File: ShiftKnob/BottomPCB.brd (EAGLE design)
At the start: 38.1 x 38 mm, 38 parts, among them IC2 UA78M05DCY, J1 AVR_SPI_PRG_6PTH, Q1 16MHz, Q2 MOSFET-NCHANNELSMD, Q3 MOSFET-PCHANNELSMD, Q4 MOSFET-NCHANNELSMD, Q5 MOSFET-NCHANNELSMD, Q6 MOSFET-NCHANNELSMD, U1 ATMEGA328, U3 FT232RL-BASICSSOP

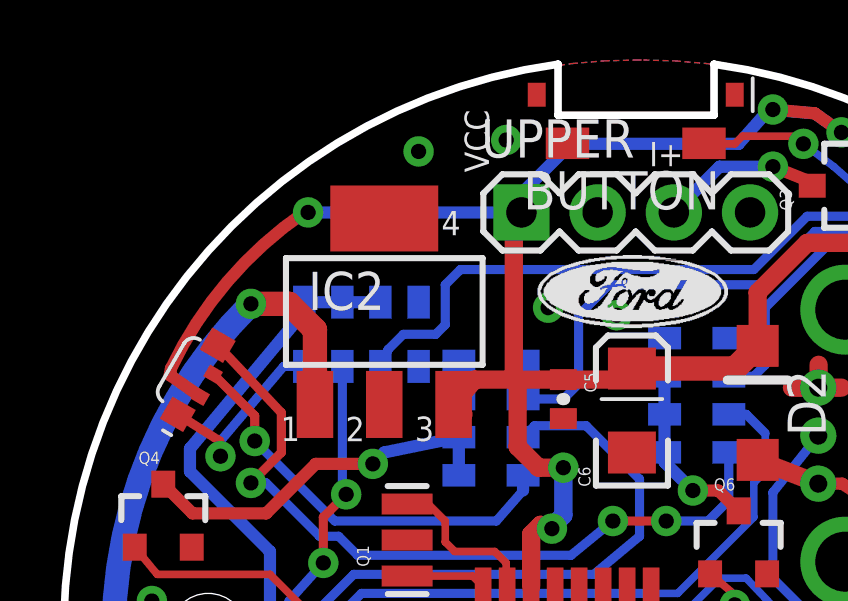
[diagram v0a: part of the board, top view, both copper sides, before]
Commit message: move silk screens for better visibility.
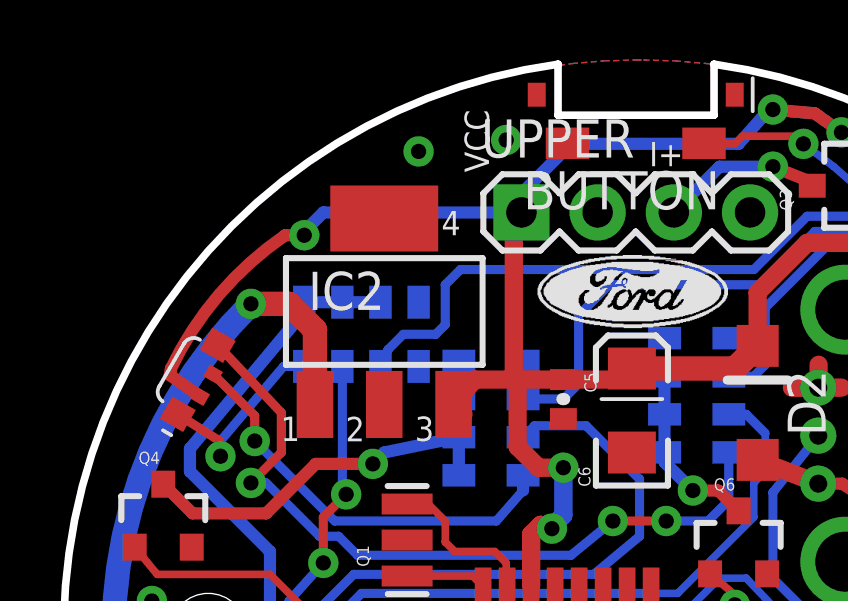
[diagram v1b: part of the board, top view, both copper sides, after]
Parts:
- moved U$3 4.27 mm to (17.7, 19.0)
- renumbered U$6 to U6
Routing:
- net GND: vias 21 -> 19
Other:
- board text added: "v02"
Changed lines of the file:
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@@
 <text x="21.778" y="6.162" size="0.8128" layer="21" rot="R180" align="bottom-right">SER</text>
 <text x="24.1402" y="22.8498" size="1.778" layer="22" rot="MR0">ZNELSON1</text>
-<text x="26.7056" y="13.3248" size="1.778" layer="22" rot="MR0">4.05.13</text>
+<text x="26.3246" y="32.5018" size="1.778" layer="22" rot="MR0">4.05.13</text>
 <rectangle x1="21.0033" y1="19.8907" x2="21.6129" y2="19.9161" layer="22" rot="R180"/>
 <rectangle x1="20.6223" y1="19.9161" x2="22.0193" y2="19.9415" layer="22" rot="R180"/>
@@
 <rectangle x1="20.5969" y1="22.2783" x2="22.0447" y2="22.3037" layer="22" rot="R180"/>
 <rectangle x1="21.0033" y1="22.3037" x2="21.6383" y2="22.3291" layer="22" rot="R180"/>
-<text x="14.671" y="33.594" size="0.8128" layer="22" rot="MR0">100Ω</text>
-<text x="15.174" y="32.319" size="0.8128" layer="22" rot="MR180">100Ω</text>
-<text x="25.085" y="32.324" size="0.8128" layer="22" rot="MR0">150Ω</text>
+<text x="14.798" y="33.467" size="0.8128" layer="22" rot="MR0">100Ω</text>
+<text x="14.92" y="29.276" size="0.8128" layer="22" rot="SMR270">100Ω</text>
+<text x="21.778" y="31.816" size="0.8128" layer="22" rot="SMR270">150Ω</text>
 <rectangle x1="57.3888" y1="23.5102" x2="57.9984" y2="23.5356" layer="49" rot="R90"/>
 <rectangle x1="56.9697" y1="23.4975" x2="58.3667" y2="23.5229" layer="49" rot="R90"/>
@@
 <text x="34.351" y="21.275" size="0.8128" layer="21" rot="R90">TX</text>
 <text x="30.795" y="21.275" size="0.8128" layer="21" rot="R90">RX</text>
+<text x="27.3406" y="17.8968" size="1.778" layer="22" rot="MR0">v02</text>
 </plain>
 <attributes>
@@
 <element name="U1" library="SparkFun" package="TQFP32-08" value="ATMEGA328" x="19.304" y="18.796" rot="R270"/>
 <element name="C2" library="SparkFun" package="0402-CAP" value="0.1uF" x="23.495" y="12.7"/>
-<element name="U$3" library="SparkFun" package="OSHW-LOGO-S" value="OSHW-LOGOS" x="21.3716" y="16.8046" rot="MR0"/>
+<element name="U$3" library="SparkFun" package="OSHW-LOGO-S" value="OSHW-LOGOS" x="17.6886" y="18.9636" rot="MR0"/>
 <element name="JP3" library="SparkFun-Connectors" package="1X02" value="12V Vehicle Connection" x="5.842" y="17.526" rot="MR270"/>
 <element name="LED2" library="FORD_frames" package="LED-RGB_SMD-RIGHTANGLE" value="LED-RGB" x="21.59" y="4.572" rot="R180"/>
@@
 <element name="J1" library="SparkFun-Connectors" package="2X3" value="AVR_SPI_PRG_6PTH" x="9.398" y="12.319" rot="R315"/>
 <element name="U3" library="SparkFun-DigitalIC" package="SSOP28DB" value="FT232RL-BASICSSOP" x="30.226" y="15.113" rot="R270"/>
-<element name="U$6" library="FORD_frames" package="USB-MINI-B_VERTICAL" value="USB-MINI-B_VERTICAL" x="28.575" y="28.1178" rot="MR0"/>
+<element name="U6" library="FORD_frames" package="USB-MINI-B_VERTICAL" value="USB-MINI-B_VERTICAL" x="28.575" y="28.1178" rot="MR0"/>
 <element name="R13" library="SparkFun" package="0402-RES" value="10K" x="32.893" y="24.638" rot="R90"/>
 <element name="R14" library="SparkFun" package="0402-RES" value="10K" x="31.496" y="24.638" rot="R90"/>
@@
 <contactref element="U3" pad="18"/>
 <contactref element="U3" pad="21"/>
-<contactref element="U$6" pad="GND"/>
+<contactref element="U6" pad="GND"/>
 <contactref element="C10" pad="C"/>
 <contactref element="IC2" pad="4"/>
@@
 <via x="14.351" y="37.592" extent="1-16" drill="0.508"/>
 <via x="17.272" y="37.973" extent="1-16" drill="0.508"/>
-<via x="20.955" y="32.131" extent="1-16" drill="0.508"/>
-<via x="18.669" y="32.385" extent="1-16" drill="0.508"/>
 <via x="31.496" y="30.861" extent="1-16" drill="0.508"/>
 <wire x1="27.686" y1="29.718" x2="26.797" y2="29.718" width="0.6096" layer="1"/>
@@
 <wire x1="19.431" y1="37.846" x2="17.78" y2="36.195" width="0.4064" layer="16"/>
 <wire x1="17.78" y1="36.195" x2="17.78" y2="35.56" width="0.4064" layer="16"/>
-<wire x1="10.668" y1="35.56" x2="17.78" y2="35.56" width="0.4064" layer="16"/>
+<wire x1="10.541" y1="34.798" x2="10.541" y2="34.925" width="0.4064" layer="16"/>
+<wire x1="10.541" y1="34.925" x2="11.176" y2="35.56" width="0.4064" layer="16"/>
+<wire x1="11.176" y1="35.56" x2="17.78" y2="35.56" width="0.4064" layer="16"/>
 <wire x1="25.654" y1="31.11" x2="24.9" y2="30.356" width="0.8128" layer="1"/>
 <wire x1="24.9" y1="30.356" x2="21.463" y2="30.356" width="0.8128" layer="1"/>
-<via x="10.668" y="35.56" extent="1-16" drill="0.508"/>
-<wire x1="10.668" y1="35.56" x2="10.541" y2="35.56" width="0.4064" layer="1"/>
-<wire x1="10.541" y1="35.56" x2="6.096" y2="30.353" width="0.4064" layer="1" curve="30"/>
+<via x="10.541" y="34.798" extent="1-16" drill="0.508"/>
+<wire x1="10.541" y1="34.798" x2="9.906" y2="34.798" width="0.4064" layer="1"/>
+<wire x1="9.906" y1="34.798" x2="6.096" y2="30.353" width="0.4064" layer="1" curve="30"/>
 <wire x1="7.07310625" y1="29.42460625" x2="6.05710625" y2="30.13789375" width="0.4064" layer="1"/>
 <wire x1="6.05710625" y1="30.13789375" x2="6.096" y2="30.353" width="0.4064" layer="1"/>
@@
 <contactref element="D2" pad="A"/>
 <contactref element="C10" pad="A"/>
-<contactref element="U$6" pad="VUSB"/>
+<contactref element="U6" pad="VUSB"/>
 <contactref element="U3" pad="20"/>
 <contactref element="U3" pad="4"/>
@@
 </signal>
 <signal name="N$21">
-<contactref element="U$6" pad="D+"/>
+<contactref element="U6" pad="D+"/>
 <contactref element="U3" pad="15"/>
 <wire x1="33.882" y1="10.888" x2="31.022" y2="10.888" width="0.3048" layer="1"/>
@@
 </signal>
 <signal name="N$22">
-<contactref element="U$6" pad="D-"/>
+<contactref element="U6" pad="D-"/>
 <contactref element="U3" pad="16"/>
 <wire x1="33.882" y1="11.538" x2="31.769" y2="11.538" width="0.3048" layer="1"/>

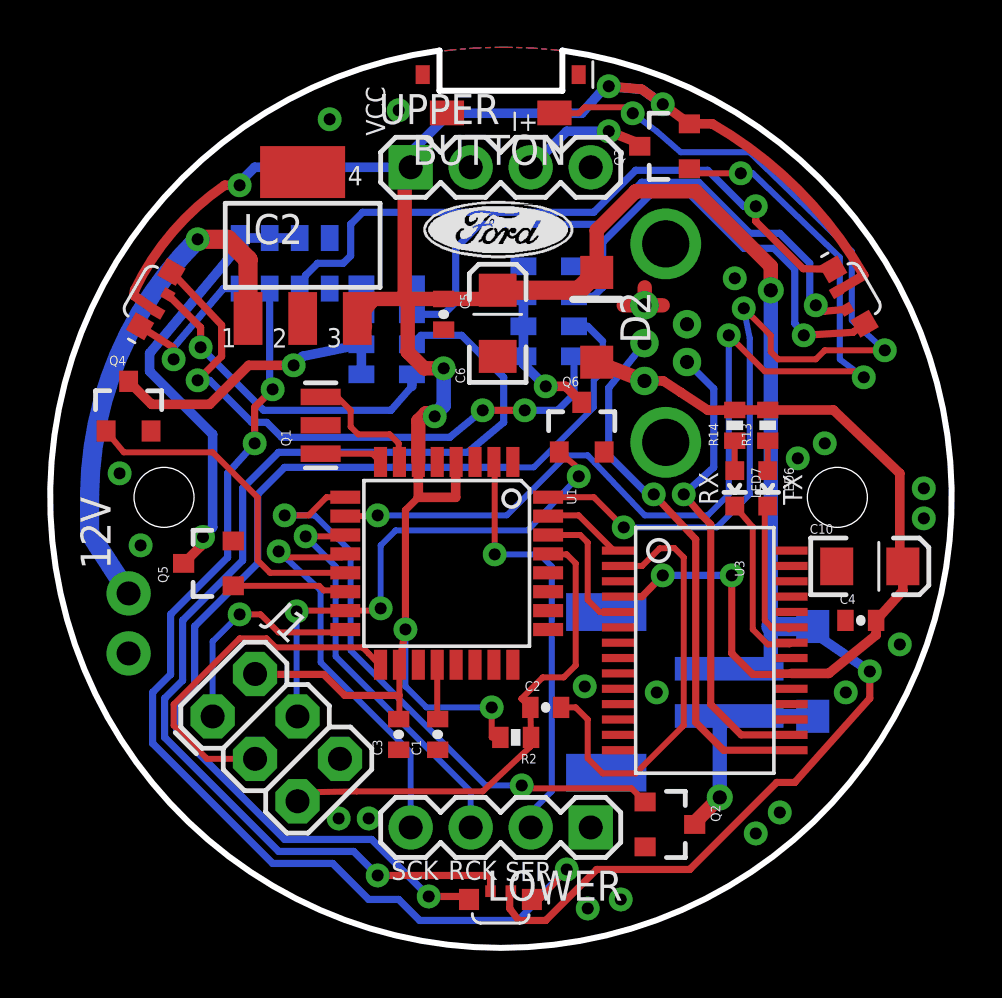
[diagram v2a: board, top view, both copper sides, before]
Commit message: fix TX/RX issue on v02 board schematic and layout.
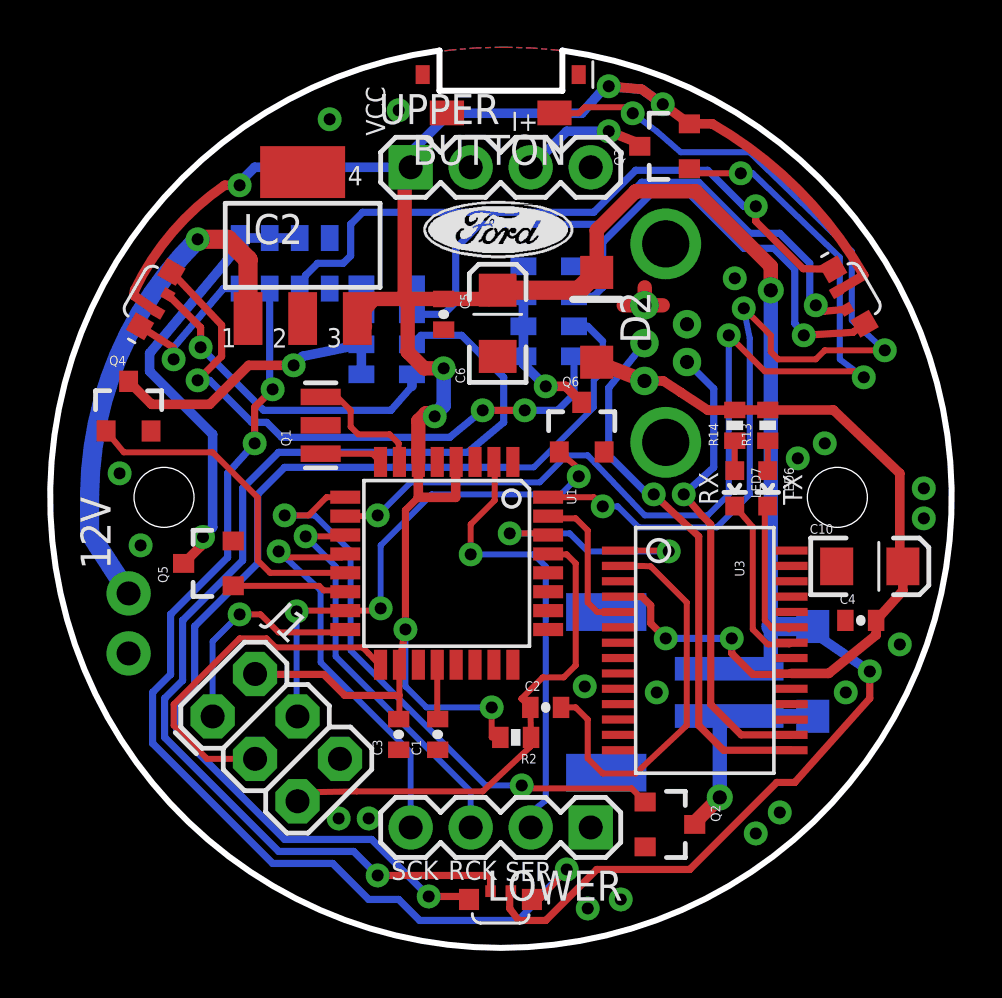
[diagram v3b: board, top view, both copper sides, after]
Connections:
- net RXI: now also U3.1; no longer U3.5
- net TXO: now also U3.5; no longer U3.1
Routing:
- net RXI: track 5.75 -> 10.9 mm, vias 0 -> 2
- net TXO: track 3.60 -> 6.44 mm
- net VUSB: track 37.3 -> 35.4 mm
- net DTR: track 18.5 -> 17.0 mm
- net D4/SERIAL: track 18.0 -> 19.1 mm
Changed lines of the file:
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@@
 <signal name="TXO">
 <contactref element="U1" pad="31"/>
-<contactref element="U3" pad="1"/>
-<wire x1="24.892" y1="20.828" x2="23.6286" y2="20.828" width="0.254" layer="1"/>
-<wire x1="23.6286" y1="20.828" x2="23.5966" y2="20.796" width="0.254" layer="1"/>
-<wire x1="24.892" y1="20.828" x2="26.382" y2="19.338" width="0.254" layer="1"/>
-<wire x1="26.382" y1="19.338" x2="26.57" y2="19.338" width="0.254" layer="1"/>
+<contactref element="U3" pad="5"/>
+<wire x1="26.57" y1="16.738" x2="25.68" y2="16.738" width="0.254" layer="1"/>
+<wire x1="25.68" y1="16.738" x2="25.273" y2="17.145" width="0.254" layer="1"/>
+<wire x1="25.273" y1="17.145" x2="25.273" y2="20.193" width="0.254" layer="1"/>
+<wire x1="25.273" y1="20.193" x2="24.765" y2="20.701" width="0.254" layer="1"/>
+<wire x1="24.765" y1="20.701" x2="23.6916" y2="20.701" width="0.254" layer="1"/>
+<wire x1="23.6916" y1="20.701" x2="23.5966" y2="20.796" width="0.254" layer="1"/>
 </signal>
 <signal name="12V" class="1">
@@
 <contactref element="BUTTON" pad="P1"/>
 <wire x1="23.5966" y1="21.596" x2="25.533" y2="21.596" width="0.254" layer="1"/>
-<wire x1="25.533" y1="21.596" x2="26.797" y2="20.32" width="0.254" layer="1"/>
-<via x="26.797" y="20.32" extent="1-16" drill="0.508"/>
-<wire x1="26.797" y1="20.32" x2="30.734" y2="20.32" width="0.254" layer="16"/>
+<wire x1="25.533" y1="21.596" x2="25.908" y2="21.209" width="0.254" layer="1"/>
+<via x="25.908" y="21.209" extent="1-16" drill="0.508"/>
+<wire x1="25.908" y1="21.209" x2="26.543" y2="21.209" width="0.254" layer="16"/>
+<wire x1="26.543" y1="21.209" x2="27.432" y2="20.32" width="0.254" layer="16"/>
+<wire x1="27.432" y1="20.32" x2="30.734" y2="20.32" width="0.254" layer="16"/>
 <wire x1="23.865" y1="37.862" x2="24.384" y2="37.846" width="0.254" layer="1"/>
 <via x="27.178" y="37.846" extent="1-16" drill="0.508"/>
@@
 <contactref element="LOWER" pad="2"/>
 <wire x1="22.86" y1="7.62" x2="22.86" y2="8.255" width="0.254" layer="16"/>
-<wire x1="22.86" y1="8.255" x2="23.749" y2="9.144" width="0.254" layer="16"/>
-<wire x1="23.749" y1="9.144" x2="23.749" y2="18.669" width="0.254" layer="16"/>
+<wire x1="22.86" y1="8.255" x2="23.495" y2="8.763" width="0.254" layer="16"/>
+<wire x1="23.495" y1="8.763" x2="23.495" y2="18.669" width="0.254" layer="16"/>
 <wire x1="21.336" y1="23.1206" x2="21.304" y2="23.0886" width="0.254" layer="1"/>
-<wire x1="23.749" y1="18.669" x2="23.241" y2="19.177" width="0.254" layer="16"/>
-<wire x1="23.241" y1="19.177" x2="21.336" y2="19.177" width="0.254" layer="16"/>
-<via x="21.336" y="19.177" extent="1-16" drill="0.508"/>
-<wire x1="21.336" y1="19.177" x2="21.336" y2="23.0566" width="0.254" layer="1"/>
+<wire x1="23.495" y1="18.669" x2="22.987" y2="19.177" width="0.254" layer="16"/>
+<wire x1="22.987" y1="19.177" x2="20.32" y2="19.177" width="0.254" layer="16"/>
+<via x="20.32" y="19.177" extent="1-16" drill="0.508"/>
+<wire x1="20.32" y1="19.177" x2="20.32" y2="20.447" width="0.254" layer="1"/>
+<wire x1="20.32" y1="20.447" x2="21.336" y2="21.463" width="0.254" layer="1"/>
+<wire x1="21.336" y1="21.463" x2="21.336" y2="23.0566" width="0.254" layer="1"/>
 <wire x1="21.336" y1="23.0566" x2="21.304" y2="23.0886" width="0.254" layer="1"/>
 </signal>
@@
 <wire x1="16.351" y1="20.796" x2="16.383" y2="20.828" width="0.254" layer="1"/>
 <via x="16.383" y="20.828" extent="1-16" drill="0.508"/>
-<wire x1="16.383" y1="20.828" x2="21.844" y2="20.828" width="0.254" layer="16"/>
-<wire x1="21.844" y1="20.828" x2="24.384" y2="23.368" width="0.254" layer="16"/>
+<wire x1="16.383" y1="20.828" x2="17.78" y2="22.225" width="0.254" layer="16"/>
+<wire x1="17.78" y1="22.225" x2="23.241" y2="22.225" width="0.254" layer="16"/>
+<wire x1="23.241" y1="22.225" x2="24.384" y2="23.368" width="0.254" layer="16"/>
 <wire x1="24.384" y1="23.368" x2="25.273" y2="23.368" width="0.254" layer="16"/>
 <wire x1="25.273" y1="23.368" x2="27.686" y2="20.828" width="0.254" layer="16"/>
@@
 <wire x1="25.908" y1="9.906" x2="27.305" y2="9.906" width="0.254" layer="1"/>
 <wire x1="26.57" y1="18.688" x2="27.578" y2="18.688" width="0.254" layer="1"/>
-<wire x1="27.578" y1="18.688" x2="28.321" y2="19.431" width="0.254" layer="1"/>
-<wire x1="28.321" y1="19.431" x2="28.937" y2="19.45" width="0.254" layer="1"/>
-<wire x1="28.937" y1="19.45" x2="29.337" y2="19.05" width="0.254" layer="1"/>
-<wire x1="29.337" y1="19.05" x2="29.337" y2="11.938" width="0.254" layer="1"/>
-<wire x1="29.337" y1="11.938" x2="27.305" y2="9.906" width="0.254" layer="1"/>
+<wire x1="27.578" y1="18.688" x2="27.94" y2="18.669" width="0.254" layer="1"/>
+<wire x1="27.94" y1="18.669" x2="29.464" y2="17.145" width="0.254" layer="1"/>
+<wire x1="29.464" y1="17.145" x2="29.464" y2="11.938" width="0.254" layer="1"/>
+<wire x1="29.464" y1="11.938" x2="27.305" y2="9.906" width="0.254" layer="1"/>
 </signal>
 <signal name="RXI">
 <contactref element="U1" pad="30"/>
-<contactref element="U3" pad="5"/>
-<wire x1="23.5966" y1="19.996" x2="24.9555" y2="19.996" width="0.254" layer="1"/>
-<wire x1="24.9555" y1="19.996" x2="25.273" y2="19.6785" width="0.254" layer="1"/>
-<wire x1="25.273" y1="19.6785" x2="25.273" y2="17.246" width="0.254" layer="1"/>
-<wire x1="25.273" y1="17.246" x2="25.781" y2="16.738" width="0.254" layer="1"/>
-<wire x1="25.781" y1="16.738" x2="26.57" y2="16.738" width="0.254" layer="1"/>
+<contactref element="U3" pad="1"/>
+<wire x1="26.57" y1="19.338" x2="28.609" y2="19.338" width="0.254" layer="1"/>
+<wire x1="28.609" y1="19.338" x2="28.702" y2="19.304" width="0.254" layer="1"/>
+<via x="28.702" y="19.304" extent="1-16" drill="0.508"/>
+<wire x1="28.702" y1="19.304" x2="25.273" y2="19.304" width="0.254" layer="16"/>
+<wire x1="25.273" y1="19.304" x2="24.511" y2="20.066" width="0.254" layer="16"/>
+<wire x1="24.511" y1="20.066" x2="21.971" y2="20.066" width="0.254" layer="16"/>
+<via x="21.971" y="20.066" extent="1-16" drill="0.508"/>
+<wire x1="21.971" y1="20.066" x2="23.368" y2="20.066" width="0.254" layer="1"/>
+<wire x1="23.368" y1="20.066" x2="23.5396" y2="19.939" width="0.254" layer="1"/>
+<wire x1="23.5396" y1="19.939" x2="23.5966" y2="19.996" width="0.254" layer="1"/>
 </signal>
 <signal name="A6">
@@
 <via x="16.51" y="16.891" extent="1-16" drill="0.508"/>
 <wire x1="16.51" y1="16.891" x2="16.51" y2="19.558" width="0.254" layer="16"/>
-<wire x1="16.51" y1="19.558" x2="17.145" y2="20.193" width="0.254" layer="16"/>
-<wire x1="17.145" y1="20.193" x2="22.733" y2="20.193" width="0.254" layer="16"/>
-<wire x1="22.733" y1="20.193" x2="24.892" y2="22.479" width="0.254" layer="16"/>
+<wire x1="16.51" y1="19.558" x2="18.669" y2="21.717" width="0.254" layer="16"/>
+<wire x1="18.669" y1="21.717" x2="24.13" y2="21.717" width="0.254" layer="16"/>
+<wire x1="24.13" y1="21.717" x2="24.892" y2="22.479" width="0.254" layer="16"/>
 <via x="24.892" y="22.479" extent="1-16" drill="0.508"/>
 <wire x1="24.892" y1="22.479" x2="24.892" y2="22.815" width="0.254" layer="1"/>
@@
 <wire x1="30.368" y1="25.273" x2="31.496" y2="25.288" width="0.4064" layer="1"/>
 <wire x1="31.496" y1="25.288" x2="32.893" y2="25.288" width="0.4064" layer="1"/>
-<wire x1="31.369" y1="14.986" x2="31.369" y2="18.288" width="0.3048" layer="1"/>
-<via x="31.369" y="18.288" extent="1-16" drill="0.508"/>
-<wire x1="31.369" y1="18.288" x2="28.448" y2="18.288" width="0.3048" layer="16"/>
-<via x="28.448" y="18.288" extent="1-16" drill="0.508"/>
-<wire x1="28.448" y1="18.288" x2="27.57" y2="17.388" width="0.3048" layer="1"/>
+<wire x1="31.369" y1="14.986" x2="31.369" y2="15.621" width="0.3048" layer="1"/>
+<via x="31.369" y="15.621" extent="1-16" drill="0.508"/>
+<wire x1="31.369" y1="15.621" x2="28.575" y2="15.621" width="0.3048" layer="16"/>
+<via x="28.575" y="15.621" extent="1-16" drill="0.508"/>
+<wire x1="28.575" y1="15.621" x2="27.94" y2="16.256" width="0.3048" layer="1"/>
+<wire x1="27.94" y1="16.256" x2="27.94" y2="17.018" width="0.3048" layer="1"/>
+<wire x1="27.94" y1="17.018" x2="27.57" y2="17.388" width="0.3048" layer="1"/>
 <wire x1="27.57" y1="17.388" x2="26.57" y2="17.388" width="0.3048" layer="1"/>
 <wire x1="32.893" y1="25.288" x2="35.672" y2="25.288" width="0.4064" layer="1"/>
@@
 <contactref element="U3" pad="15"/>
 <wire x1="33.882" y1="10.888" x2="31.022" y2="10.888" width="0.3048" layer="1"/>
-<wire x1="31.022" y1="10.888" x2="29.845" y2="12.065" width="0.3048" layer="1"/>
+<wire x1="31.022" y1="10.888" x2="29.972" y2="11.938" width="0.3048" layer="1"/>
 <wire x1="26.162" y1="23.368" x2="26.162" y2="26.2238" width="0.3048" layer="16"/>
 <wire x1="26.162" y1="26.2238" x2="27.675" y2="28.1178" width="0.3048" layer="16"/>
-<wire x1="29.845" y1="12.065" x2="29.845" y2="19.812" width="0.3048" layer="1"/>
-<wire x1="29.845" y1="19.812" x2="28.067" y2="21.717" width="0.3048" layer="1"/>
+<wire x1="29.972" y1="11.938" x2="29.972" y2="19.939" width="0.3048" layer="1"/>
+<wire x1="29.972" y1="19.939" x2="28.067" y2="21.717" width="0.3048" layer="1"/>
 <via x="28.067" y="21.717" extent="1-16" drill="0.508"/>
 <wire x1="28.067" y1="21.717" x2="27.813" y2="21.717" width="0.3048" layer="16"/>
